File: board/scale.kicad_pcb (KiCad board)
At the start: 2 copper layers, 40 x 70 mm, 54 parts, among them J1 Cell A, J2 Cell B, J3 Cell C, J4 Cell D, J5 Jack-DC, J6 Conn_01x05, Q1 Q_PNP_BCE, SW1 SW_Push, U1 HX711, U2 ESP-12E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

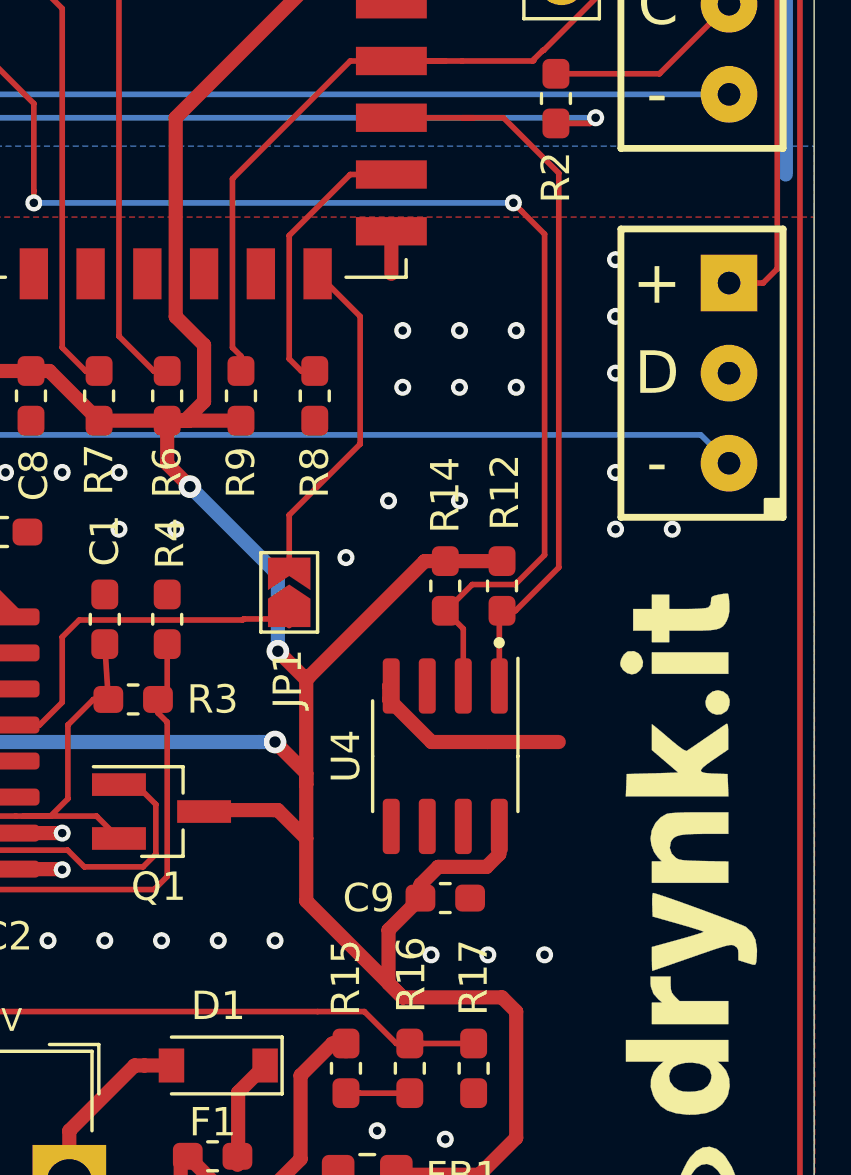
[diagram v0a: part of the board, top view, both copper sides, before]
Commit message: Place resistor for TMP75
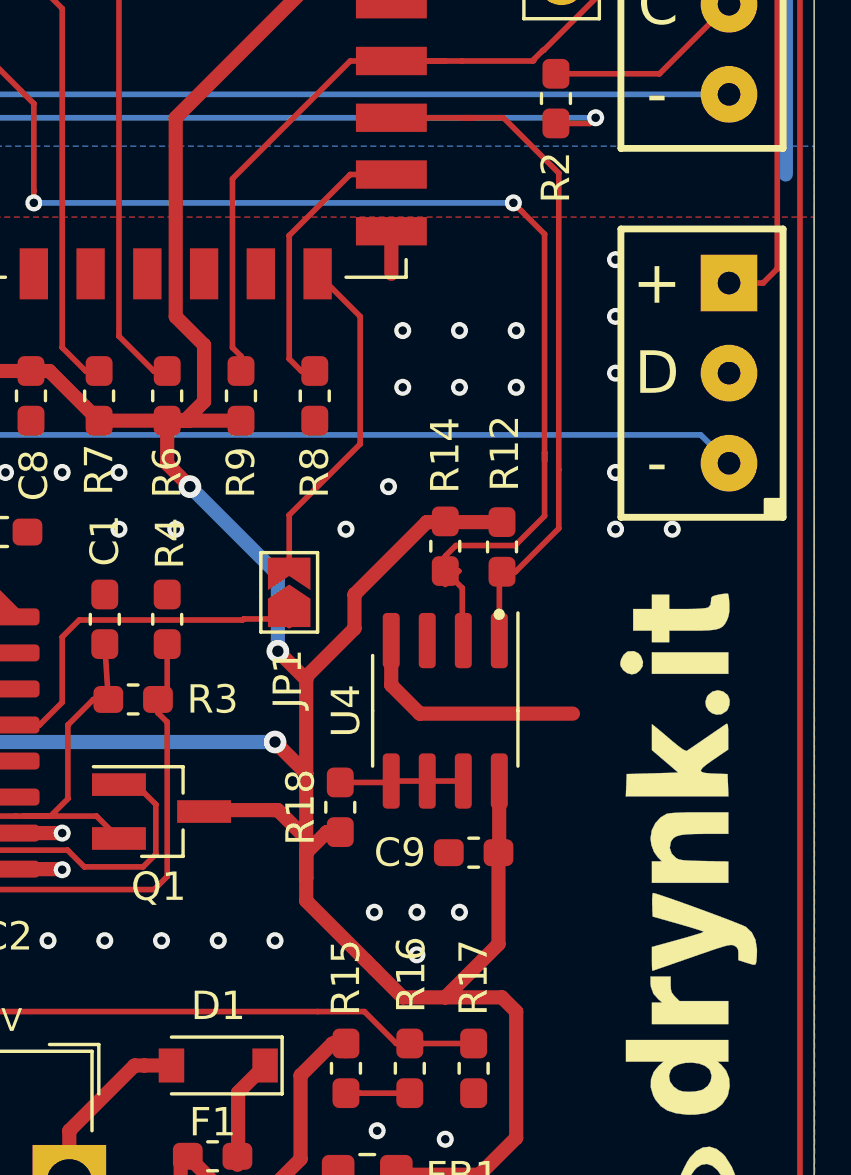
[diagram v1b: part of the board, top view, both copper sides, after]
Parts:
- added R18: 4.7k, Resistor_SMD:R_0603_1608Metric_Pad1.05x0.95mm_HandSolder, F.Cu at (40.3, 60.3)
- moved C9 1.89 mm to (45.0, 61.9), turned to 180 degrees
- moved U4 1.60 mm to (44.0, 56.9)
- moved R14 1.40 mm to (44.0, 51.1)
- moved R12 1.38 mm to (46.0, 51.1)
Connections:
- U4 pad 5: Net-(U4-Pad5) -> Net-(R18-Pad1)
- U4 pad 6: Net-(U4-Pad6) -> Net-(R18-Pad1)
- U4 pad 7: Net-(U4-Pad7) -> Net-(R18-Pad1)
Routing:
- net Net-(R18-Pad1): track 0.00 -> 4.36 mm
- net +3V3: track 144.3 -> 147.6 mm
- net /SDA: track 26.3 -> 24.7 mm
- net GND: track 41.5 -> 42.7 mm
